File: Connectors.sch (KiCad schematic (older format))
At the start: 27 parts, among them J400 Conn_01x02, J401 SWD, J402 USB_B_Micro, J403 Conn_01x04, J404 Conn_01x04, J405 Conn_01x04, J406 Conn_01x04, J407 Conn_01x04, J408 Conn_01x04, U400 USBLC6-2SC6

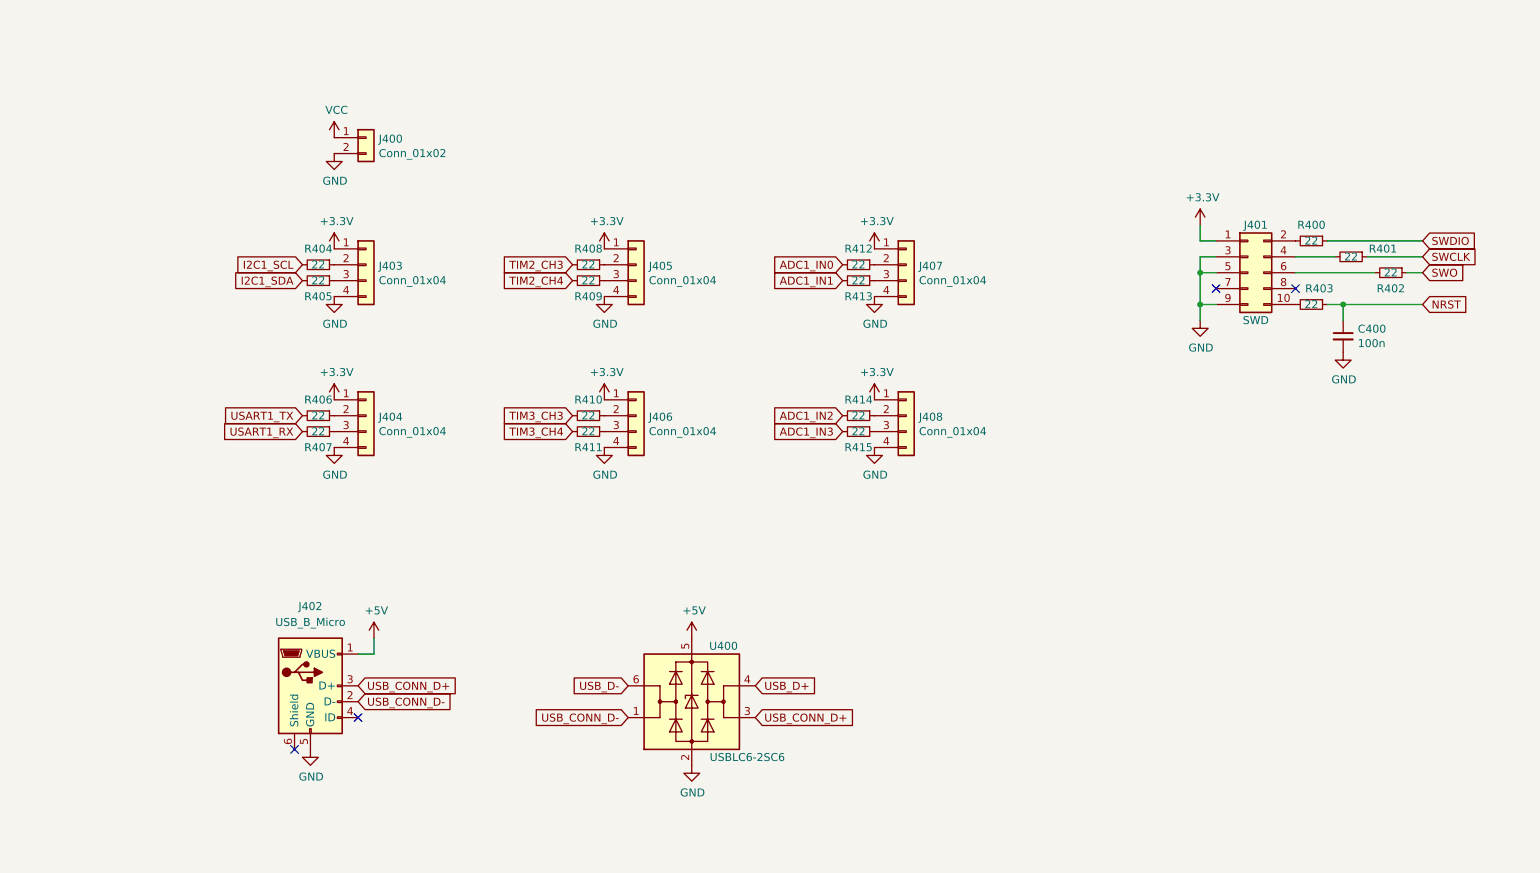
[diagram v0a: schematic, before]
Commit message: Updated firmware. Added schematic PDF.
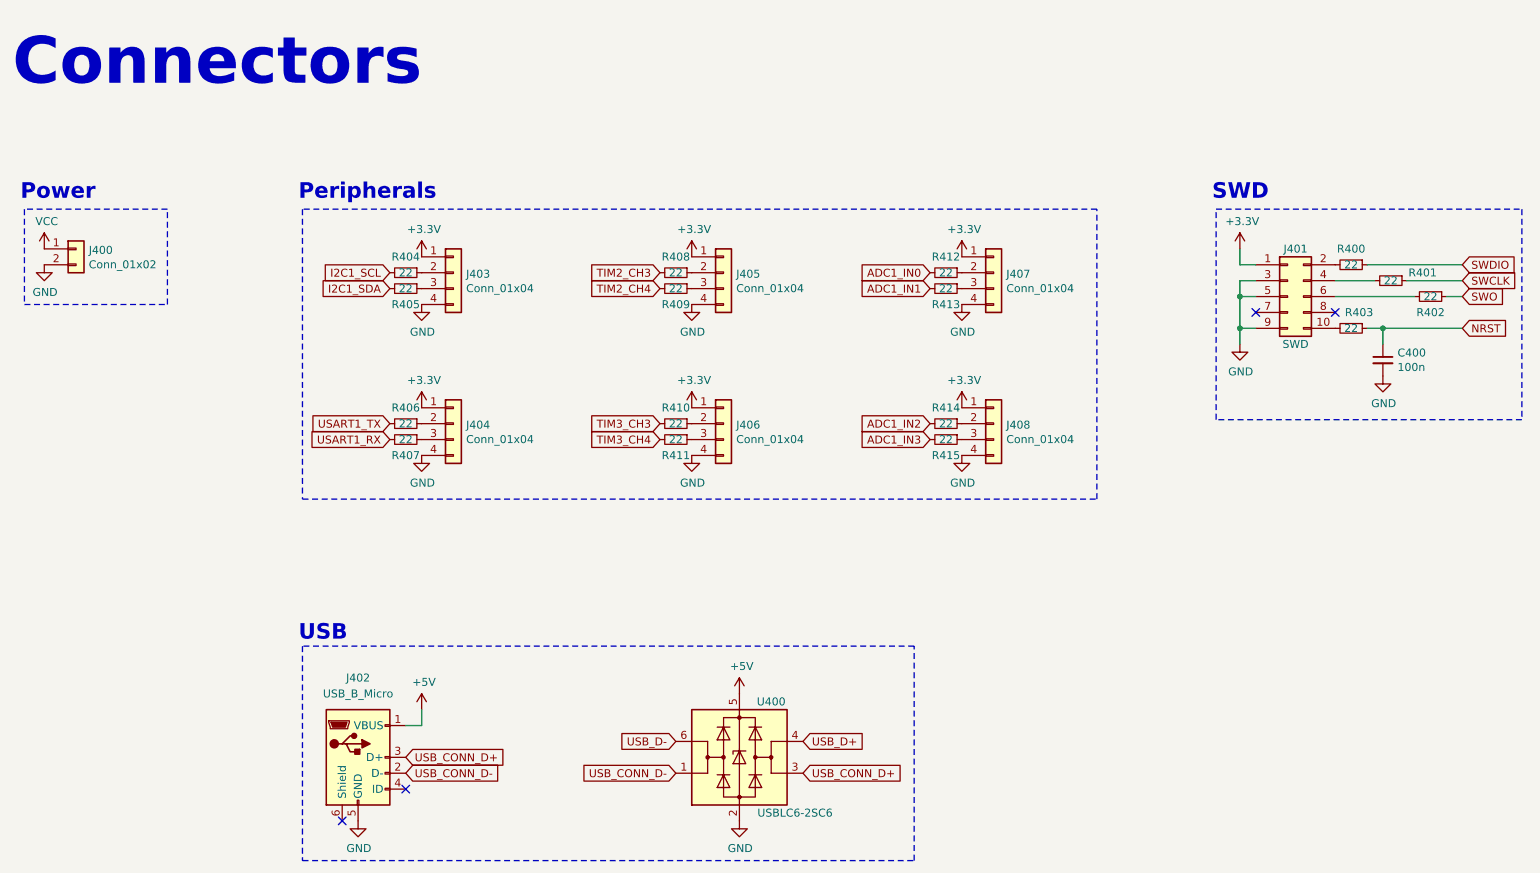
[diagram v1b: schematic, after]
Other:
- note added: "Connectors"
- note added: "Peripherals"
- note added: "Power"
- note added: "SWD"
- note added: "USB"
- moved on the sheet: C400, J400, J401, J402, J403, J404, J405, J406, J407, J408, R400, R401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

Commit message: Changed USB connector.
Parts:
- removed U400: USBLC6-2SC6, Package_TO_SOT_SMD:SOT-23-6, symbol Power_Protection:USBLC6-2SC6
- J402: footprint SchmillipKiCADLibrary:USB_MICRO_B_101181930001LF -> Connector_USB:USB_Micro-B_Wuerth_629105150521; symbol Connector:USB_B_Micro -> RBoard-rescue:USB_B_Micro-Connector
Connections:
- net USB_CONN_D+ is gone; now on net USB_D+: J402.3 (D+)
- net USB_CONN_D- is gone; now on net USB_D-: J402.2 (D-)
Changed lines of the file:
@@
 Connection ~ 9550 2750
 $Comp
-L Connector:USB_B_Micro J402
+L RBoard-rescue:USB_B_Micro-Connector J402
 U 1 1 5F9F2004
 P 3100 5450
+AR Path="/5F9F2004" Ref="J402"  Part="1"
+AR Path="/5F83C1A4/5F9F2004" Ref="J402"  Part="1"
 F 0 "J402" H 3100 5950 50  0000 C CNN
 F 1 "USB_B_Micro" H 3100 5850 50  0000 C CNN
-F 2 "SchmillipKiCADLibrary:USB_MICRO_B_101181930001LF" H 3250 5400 50  0001 C CNN
+F 2 "Connector_USB:USB_Micro-B_Wuerth_629105150521" H 3250 5400 50  0001 C CNN
 F 3 "~" H 3250 5400 50  0001 C CNN
 	1    3100 5450
@@
 $EndComp
 NoConn ~ 3400 5650
-Text GLabel 3400 5450 2    50   Input ~ 0
-USB_CONN_D+
-Text GLabel 3400 5550 2    50   Input ~ 0
-USB_CONN_D-
 $Comp
 L power:+5V #PWR058
@@
 Wire Wire Line
 	3500 5250 3400 5250
-$Comp
-L Power_Protection:USBLC6-2SC6 U400
-U 1 1 5F9F4D7E
-P 5500 5450
-F 0 "U400" H 5700 5800 50  0000 C CNN
-F 1 "USBLC6-2SC6" H 5850 5100 50  0000 C CNN
-F 2 "Package_TO_SOT_SMD:SOT-23-6" H 5500 4950 50  0001 C CNN
-F 3 "https://www.st.com/resource/en/datasheet/usblc6-2.pdf" H 5700 5800 50  0001 C CNN
-F 4 "C7519" H 5500 5450 50  0001 C CNN "LCSC Part #"
-	1    5500 5450
-	1    0    0    -1
-$EndComp
-$Comp
-L power:+5V #PWR063
-U 1 1 5F9F5FCC
-P 5500 5050
-F 0 "#PWR063" H 5500 4900 50  0001 C CNN
-F 1 "+5V" H 5515 5223 50  0000 C CNN
-F 2 "" H 5500 5050 50  0001 C CNN
-F 3 "" H 5500 5050 50  0001 C CNN
-	1    5500 5050
-	1    0    0    -1
-$EndComp
-$Comp
-L power:GND #PWR064
-U 1 1 5F9F6CF1
-P 5500 5850
-F 0 "#PWR064" H 5500 5600 50  0001 C CNN
-F 1 "GND" H 5505 5677 50  0000 C CNN
-F 2 "" H 5500 5850 50  0001 C CNN
-F 3 "" H 5500 5850 50  0001 C CNN
-	1    5500 5850
-	1    0    0    -1
-$EndComp
-Text GLabel 5100 5550 0    50   Input ~ 0
-USB_CONN_D-
-Text GLabel 5900 5550 2    50   Input ~ 0
-USB_CONN_D+
-Text GLabel 5100 5350 0    50   Input ~ 0
+Text GLabel 3400 5550 2    50   Input ~ 0
 USB_D-
-Text GLabel 5900 5350 2    50   Input ~ 0
+Text GLabel 3400 5450 2    50   Input ~ 0
 USB_D+
 $Comp
@@
 	2750 2000 2750 3825
 Wire Notes Line
-	2750 6100 6600 6100
-Wire Notes Line
-	6600 6100 6600 4750
-Wire Notes Line
-	6600 4750 2750 4750
+	3850 6100 3850 4750
 Wire Notes Line
 	2750 4750 2750 6100
@@
 Text Notes 8475 1950 0    98   ~ 20
 SWD
+Wire Notes Line
+	2750 6100 3850 6100
+Wire Notes Line
+	2750 4750 3850 4750
 $EndSCHEMATC
